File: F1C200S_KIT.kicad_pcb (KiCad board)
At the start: 2 copper layers, 52 x 32.5 mm, 89 parts, among them J1 10.0402_LCD_RGB_CON_WJQ, J2 10.0002_USB_Micro, J3 10.0001_Micro_SD_Card, J4 10.0201_PH2X15_2D54_V, J5 10.0002_USB_Micro, J6 10.0202_PH2X9_2D54_V, SW1 11.0101_SW-A03-08, U1 08.0001_F1C200S, U2 09.0103_XC6206, U3 09.0102_EA3036, U4 09.0001_CP2104, U5 09.0303_GD5F1GQ4, U6 09.0302_W25Q128JVS, Y1 07.0403_Crystal_24M_3225

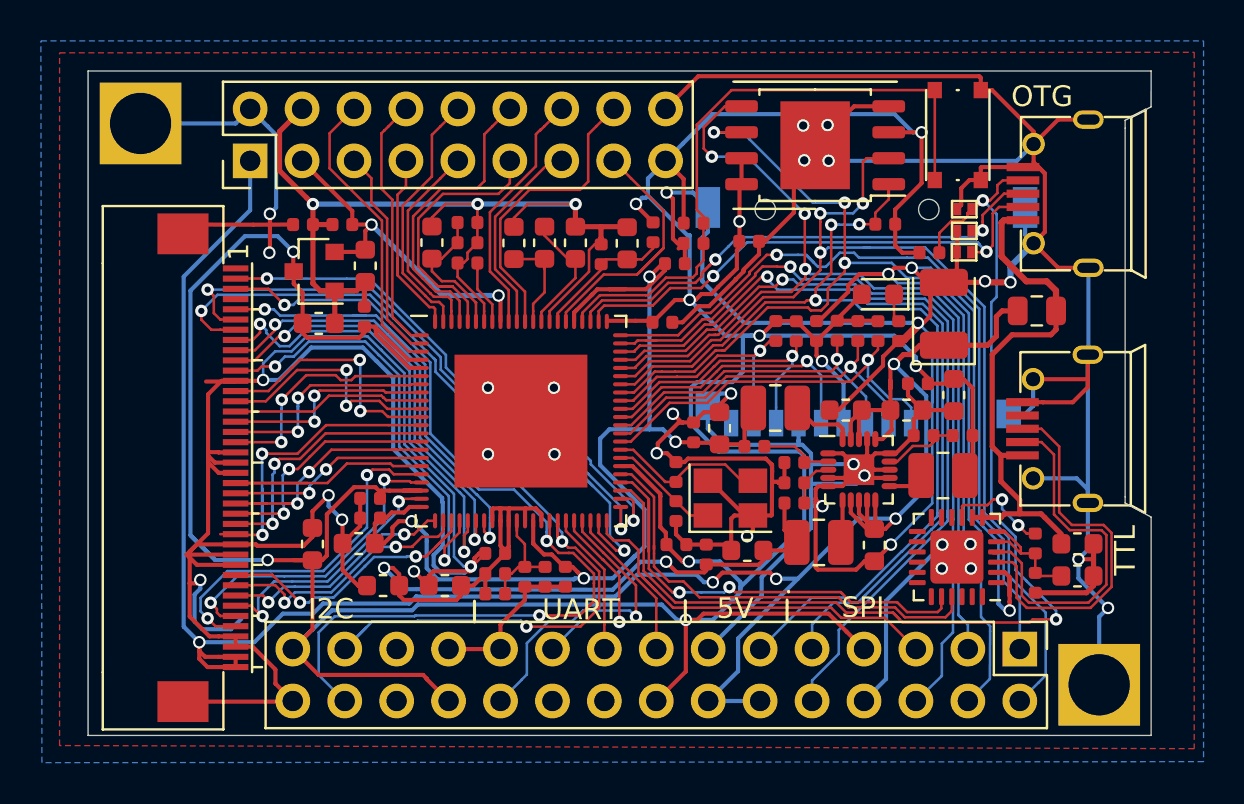
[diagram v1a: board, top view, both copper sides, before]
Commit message: 优化封装外形丝印，PCB进行拼板处理
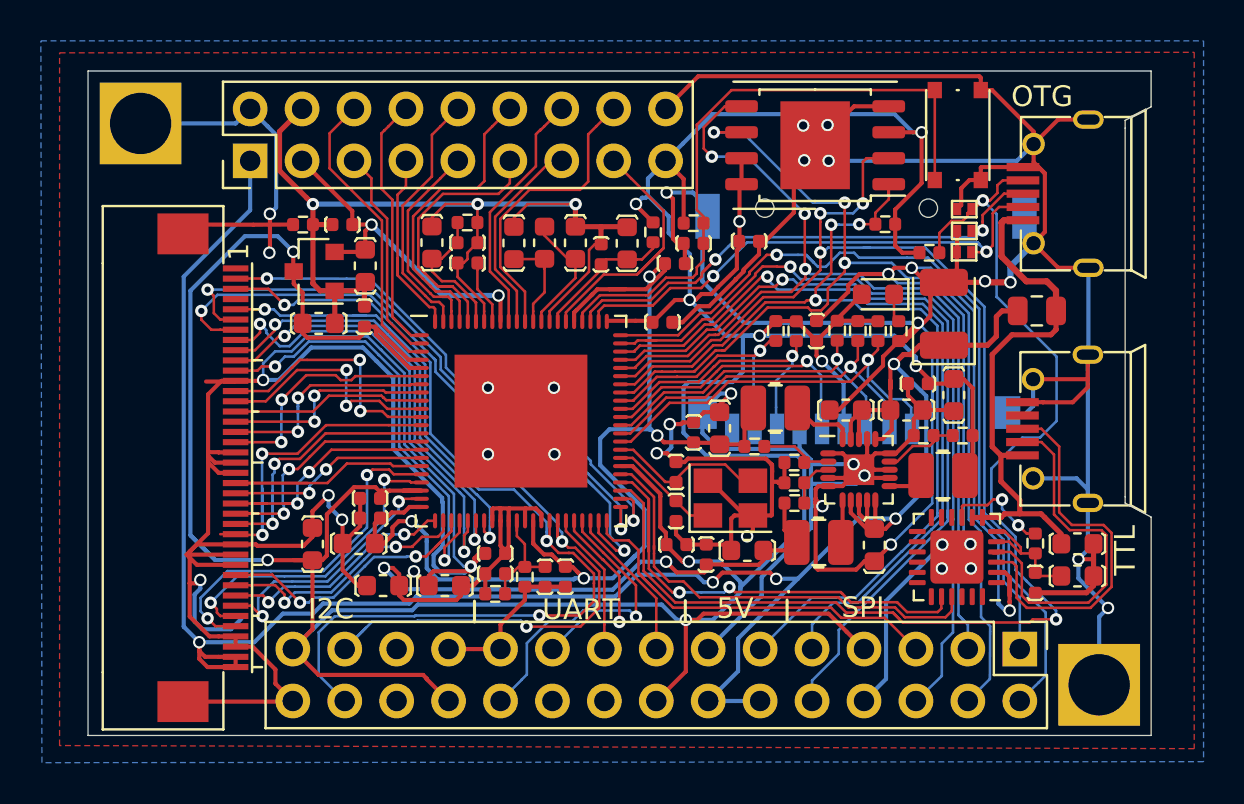
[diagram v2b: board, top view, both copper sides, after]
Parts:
- C1, C12, C2, C21, C22, C23, C27, C28, C29, C41, C5: value 03.0016_C0603_10uF -> 03.4004_C0603_10uF; footprint Capacitor_SMD:C_0603_1608Metric -> 0WJQ:C_0603_WJQ
- C10, C13, C14, C15, C16, C17, C18, C20, C24, C25, C26, C3, C34, C36, C37, C38, C4, C40, C42, C6, C7, C8, C9: footprint Capacitor_SMD:C_0402_1005Metric -> 0WJQ:C_0402_WJQ
- C11: value 03.0011_C0603_1uF -> 03.4004_C0603_10uF; footprint Capacitor_SMD:C_0603_1608Metric -> 0WJQ:C_0603_WJQ
- C19: value 03.0015_C0603_4.7uF -> 03.4004_C0603_10uF; footprint Capacitor_SMD:C_0603_1608Metric -> 0WJQ:C_0603_WJQ
- C31: value 03.0011_C0603_1uF -> 03.4001_C0603_1uF; footprint Capacitor_SMD:C_0603_1608Metric -> 0WJQ:C_0603_WJQ
- C33: value 03.0012_C0603_2.2uF -> 03.4002_C0603_2.2uF; footprint Capacitor_SMD:C_0603_1608Metric -> 0WJQ:C_0603_WJQ
- C39, C43, C45: value 03.0015_C0603_4.7uF -> 03.4003_C0603_4.7uF; footprint Capacitor_SMD:C_0603_1608Metric -> 0WJQ:C_0603_WJQ
- L1, L2, L3: footprint Inductor_SMD:L_1008_2520Metric -> 0WJQ:L_1008_2520_WJQ
- R1, R10, R11, R13, R14, R15, R16, R17, R18, R19, R2, R20, R21, R22, R3, R4, R5, R6, R7, R8, R9: footprint Resistor_SMD:R_0402_1005Metric -> 0WJQ:R_0402_WJQ
- moved J3 1.62 mm to (178.1, 110.1)
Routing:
- net /CPU/USB_ID: track 55.5 -> 58.5 mm
- net GND: track 437.9 -> 439.4 mm
- net +3V3: track 218.1 -> 218.8 mm
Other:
- board text added: "F1C200S V1.1"
- board text removed: "F1C200S V1.0"

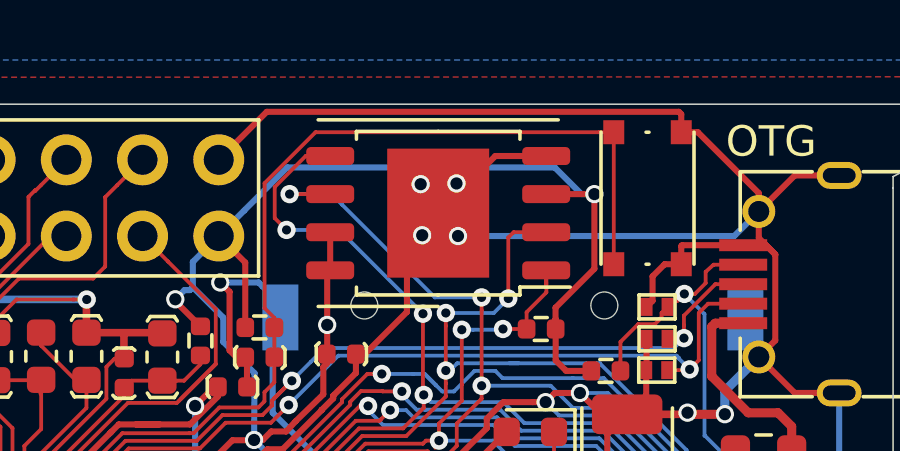
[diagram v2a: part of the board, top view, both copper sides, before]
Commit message: 修改靠近板边的地线，解决锣板掏线问题
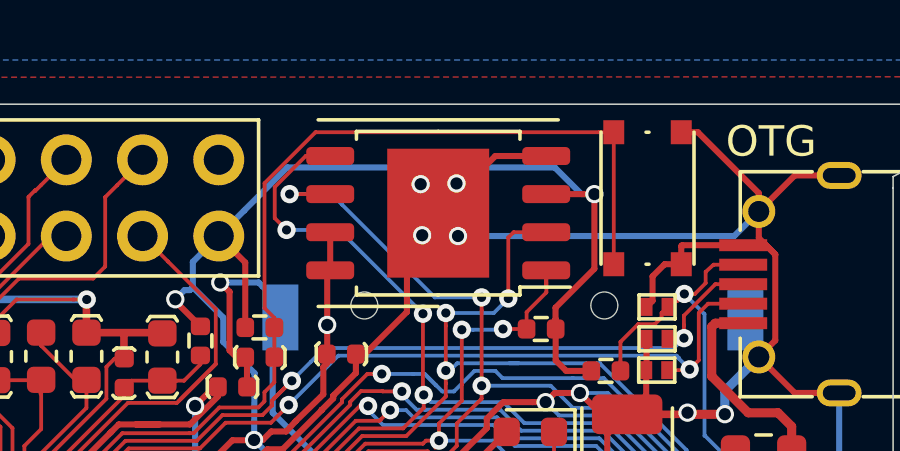
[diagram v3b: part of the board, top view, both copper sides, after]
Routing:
- net GND: track 439.4 -> 422.7 mm
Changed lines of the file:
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@@
     (thickness 1.6)
     (drawings 22)
-    (tracks 2239)
+    (tracks 2235)
     (zones 0)
     (modules 89)
@@
   (segment (start 178.4604 123.9774) (end 179.2732 123.1646) (width 0.2032) (layer F.Cu) (net 1))
   (segment (start 179.2732 123.1646) (end 179.434338 123.1646) (width 0.127) (layer B.Cu) (net 1))
-  (segment (start 168.2496 101.854) (end 169.84959 100.25401) (width 0.2032) (layer F.Cu) (net 1))
-  (segment (start 183.6674 100.3306) (end 183.6674 100.9338) (width 0.2032) (layer F.Cu) (net 1))
-  (segment (start 183.59081 100.25401) (end 183.6674 100.3306) (width 0.2032) (layer F.Cu) (net 1))
-  (segment (start 169.84959 100.25401) (end 183.59081 100.25401) (width 0.2032) (layer F.Cu) (net 1))
   (segment (start 182.499 109.7026) (end 181.864 110.3376) (width 0.2032) (layer F.Cu) (net 1))
   (segment (start 182.499 108.8644) (end 182.499 109.7026) (width 0.2032) (layer F.Cu) (net 1))
